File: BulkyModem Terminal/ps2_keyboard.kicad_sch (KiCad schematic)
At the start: 5 parts, among them J6 PS/2_Connector

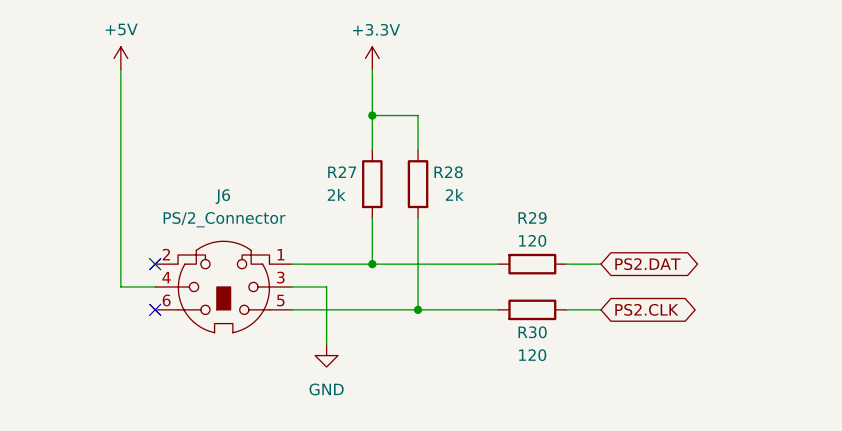
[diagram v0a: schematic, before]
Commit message: Change PS/2 circuit
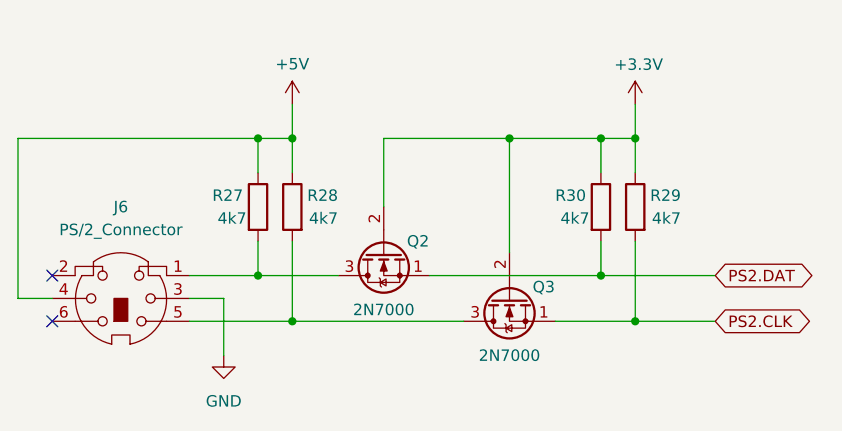
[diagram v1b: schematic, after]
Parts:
- added Q2, Q3: 2N7000, Package_TO_SOT_THT:TO-92_Inline_Wide, symbol Transistor_FET:2N7000
- R27, R28: value 2k -> 4k7
- R29, R30: value 120 -> 4k7
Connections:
- net +3.3V: now also R29.1, R30.1, Q2.2 (G), Q3.2 (G); no longer R27.1, R28.1
- net +5V: now also R27.1, R28.1
- net PS2.CLK: now also R29.2, Q3.1 (S); no longer R30.1
- net PS2.DAT: now also R30.2, Q2.1 (S); no longer R29.1
- net at J6.5, R28.2: now also Q3.3 (D); no longer R30.2
- net at J6.1, R27.2: now also Q2.3 (D); no longer R29.2
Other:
- moved on the sheet: J6, R27, R28
